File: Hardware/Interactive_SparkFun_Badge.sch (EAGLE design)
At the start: 30 parts, among them J1 AVR_SPI_PRG_6PTH, U1 ATMEGA328P

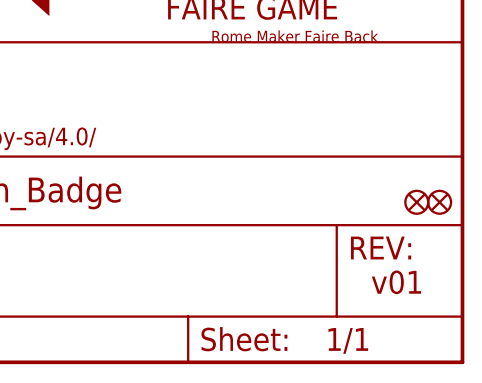
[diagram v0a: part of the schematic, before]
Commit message: Fixing version number to v10
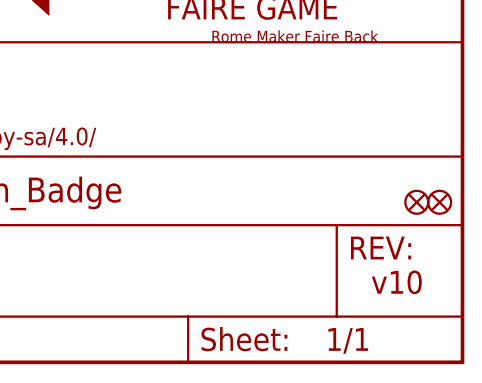
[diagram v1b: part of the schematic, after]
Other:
- note added: "v10"
- note removed: "v01"
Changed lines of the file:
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@@
 <sheet>
 <plain>
-<text x="238.76" y="7.62" size="2.54" layer="94">v01</text>
+<text x="238.76" y="7.62" size="2.54" layer="94">v10</text>
 <text x="166.116" y="11.43" size="2.54" layer="94">Toni Klopfenstein</text>
 <wire x1="0" y1="114.3" x2="58.42" y2="114.3" width="0" layer="94" style="shortdash"/>

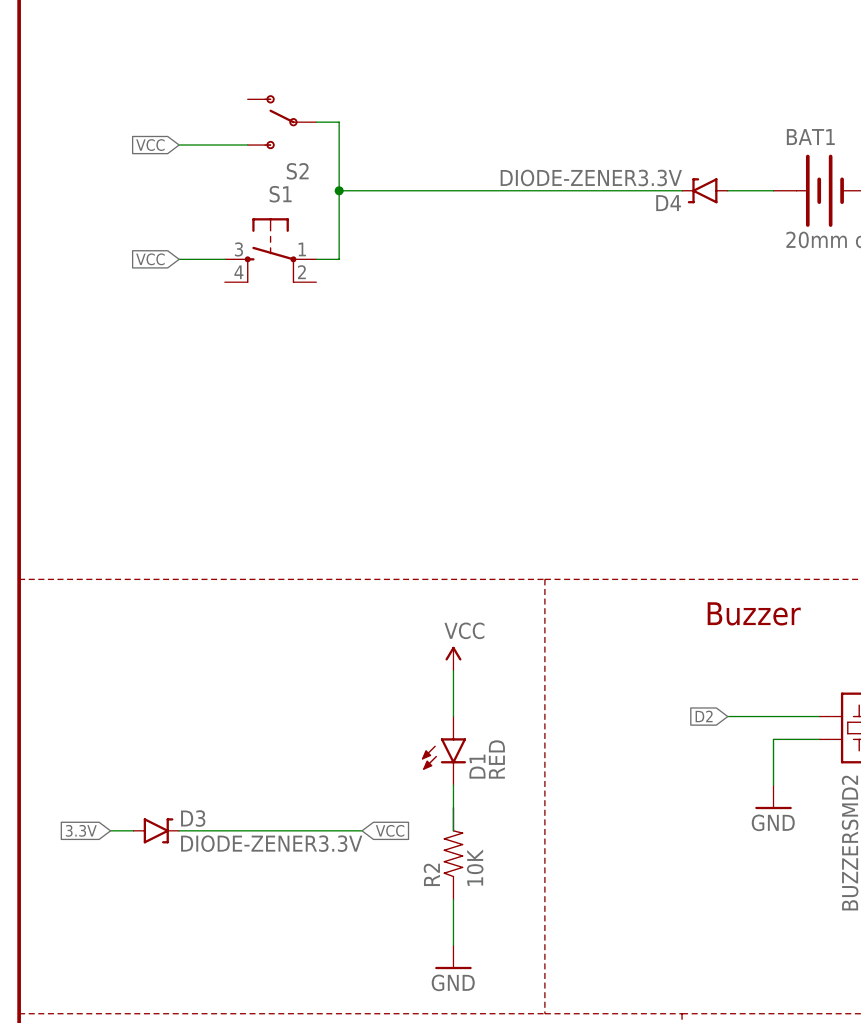
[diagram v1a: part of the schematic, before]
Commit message: Switching to Schottky diode
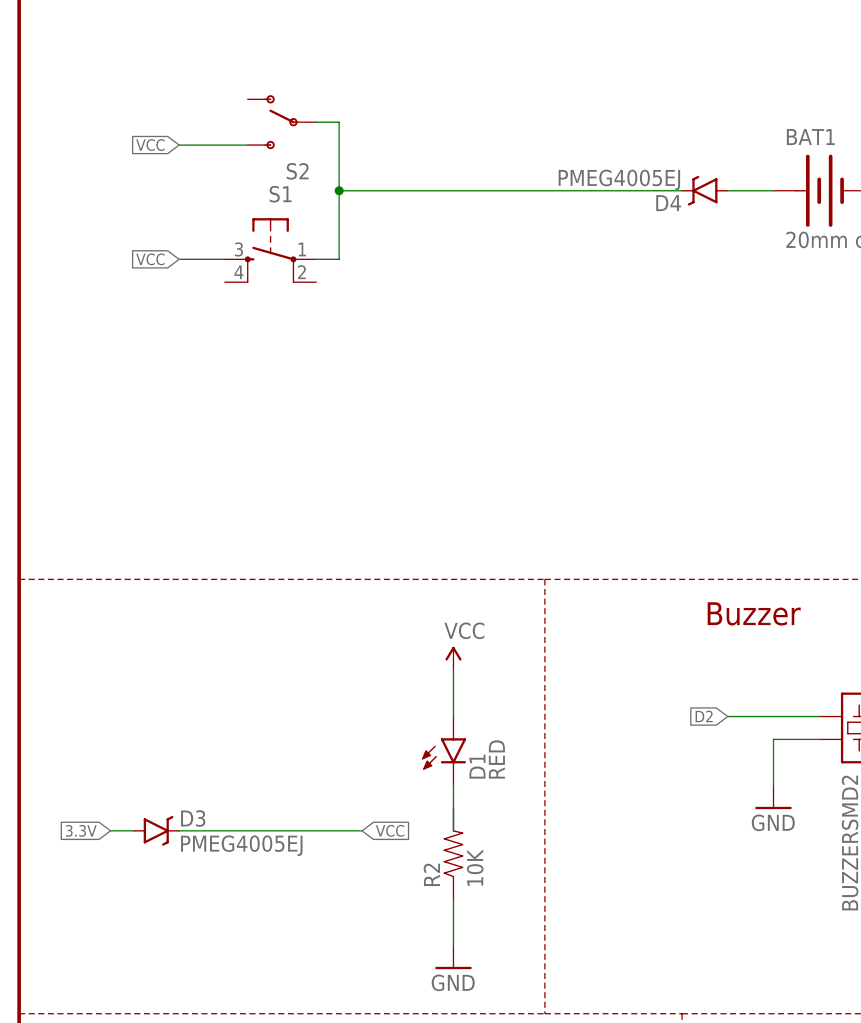
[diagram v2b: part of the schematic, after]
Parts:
- D3, D4: value DIODE-ZENER3.3V -> PMEG4005EJ; device SparkFun-DiscreteSemi:DIODE-ZENER3.3V -> SparkFun-DiscreteSemi:DIODE-SCHOTTKY-PMEG4005EJ
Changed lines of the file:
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@@
 <part name="J1" library="SparkFun-Connectors" deviceset="AVR_SPI_PRG_6" device="PTH" value="AVR_SPI_PRG_6PTH"/>
 <part name="U$3" library="ML8511" deviceset="ALPHABET" device=""/>
-<part name="D3" library="SparkFun-DiscreteSemi" deviceset="DIODE-ZENER" device="3.3V"/>
-<part name="D4" library="SparkFun-DiscreteSemi" deviceset="DIODE-ZENER" device="3.3V"/>
+<part name="D3" library="SparkFun-DiscreteSemi" deviceset="DIODE-SCHOTTKY" device="-PMEG4005EJ" value="PMEG4005EJ"/>
+<part name="D4" library="SparkFun-DiscreteSemi" deviceset="DIODE-SCHOTTKY" device="-PMEG4005EJ" value="PMEG4005EJ"/>
 <part name="C1" library="SparkFun-Capacitors" deviceset="0.1UF-25V(+80/-20%)(0603)" device="" value="0.1uF"/>
 <part name="S1" library="SparkFun-Electromechanical" deviceset="TAC_SWITCH" device="SMD"/>
